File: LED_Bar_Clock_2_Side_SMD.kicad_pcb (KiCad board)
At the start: 2 copper layers, 100 x 100 mm, 52 parts, among them J1 U262-16XN-4BVC11, J2 AVR-ISP-6, SW1 SKHMQKE010, SW2 SW_5_Way, U1 ATtiny84A-SSUR, U2 DS1307Z+, Y1 32.768 kHz

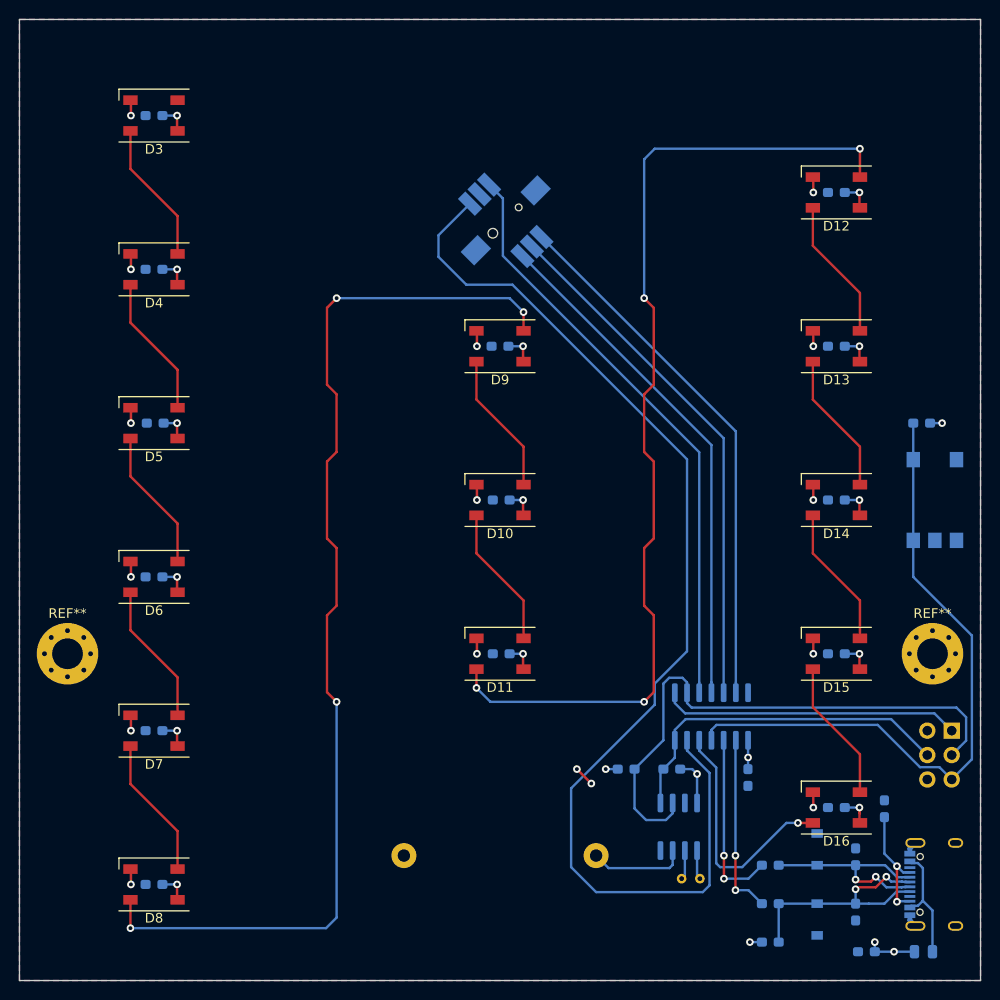
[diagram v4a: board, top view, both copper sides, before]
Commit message: Fix led and trace alignment
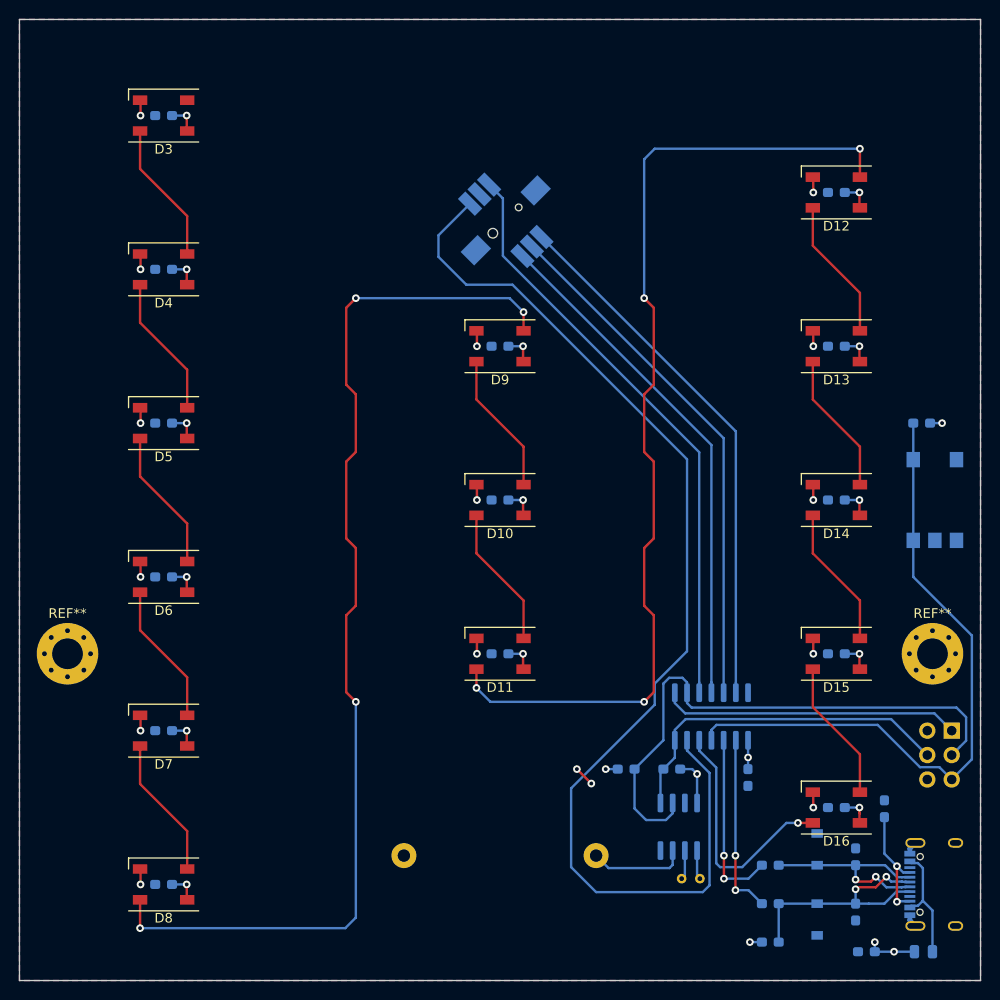
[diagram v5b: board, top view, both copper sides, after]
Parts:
- moved C4 1.00 mm to (65.0, 60.0)
- moved C5 1.00 mm to (65.0, 76.0)
- moved C7 1.00 mm to (65.0, 108.0)
- moved C8 1.00 mm to (65.0, 124.0)
- moved C9 1.00 mm to (65.0, 140.0)
- moved D3 1.00 mm to (65.0, 60.0)
- moved D4 1.00 mm to (65.0, 76.0)
- moved D5 1.00 mm to (65.0, 92.0)
- moved D6 1.00 mm to (65.0, 108.0)
- moved D7 1.00 mm to (65.0, 124.0)
- moved D8 1.00 mm to (65.0, 140.0)
- moved C6 0.88 mm to (65.0, 92.0)
- moved C11 0.12 mm to (100.0, 100.0)
- moved C12 0.12 mm to (100.0, 116.0)
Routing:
- net Net-(D8-Pad2): track 113.8 -> 112.8 mm

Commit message: Center 5 way switch
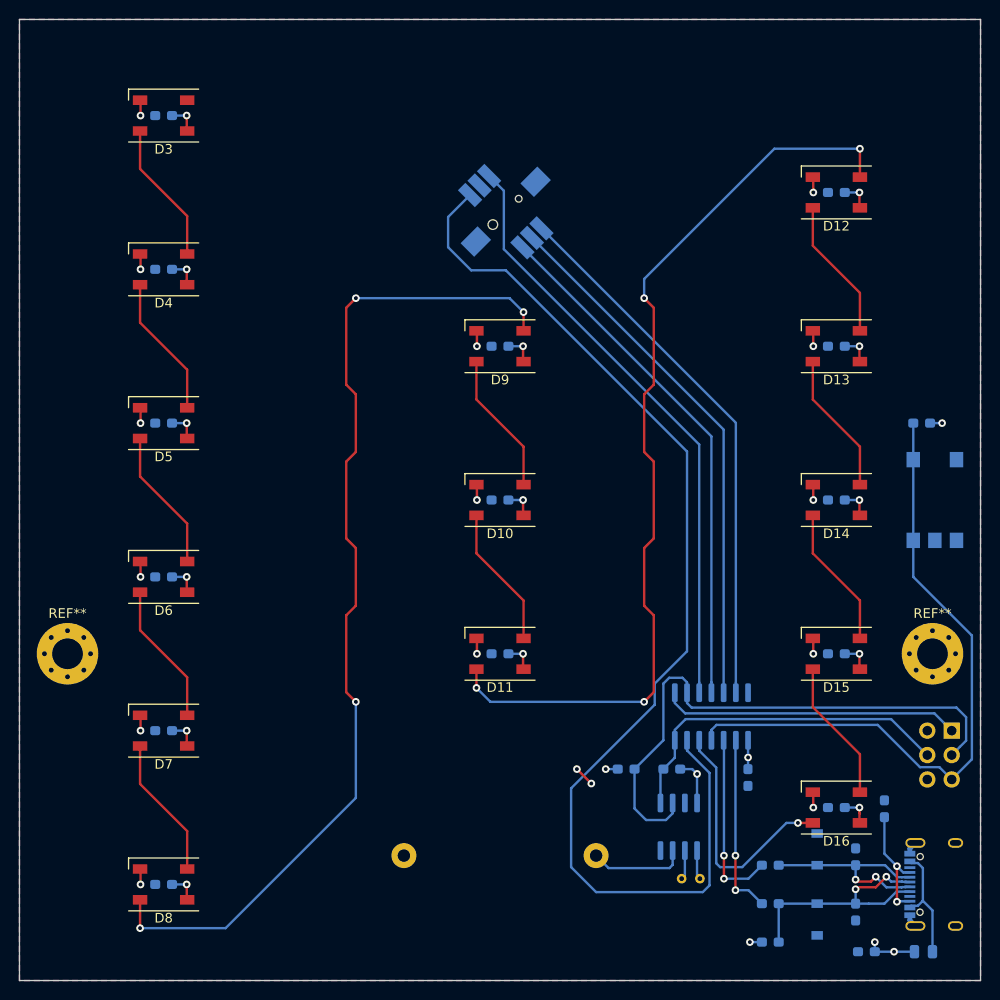
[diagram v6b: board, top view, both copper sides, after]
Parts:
- moved SW2 0.90 mm to (100.6, 70.0)
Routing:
- net Net-(D8-Pad2): track 112.8 -> 105.5 mm
- net Net-(D11-Pad2): track 104.8 -> 97.5 mm
- net Net-(SW2-Pad4): track 61.9 -> 62.8 mm
- net Net-(SW2-Pad3): track 53.6 -> 54.5 mm
- net Net-(SW2-Pad2): track 54.7 -> 55.6 mm
- net Net-(SW2-Pad1): track 55.8 -> 56.7 mm
- net Net-(SW2-Pad6): track 120.7 -> 120.1 mm
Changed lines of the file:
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@@
   )
   (module Clock_Footprints:K1-5203UA-01 (layer B.Cu)
-    (at 100.6 70.9 315)
+    (at 100.6 70 315)
     (fp_text reference SW2 (at 0.059999 0 315) (layer B.SilkS)
       (effects (font (size 1 1) (thickness 0.15)) (justify mirror))
@@
   (segment (start 102.45 82.4) (end 102.45 80.45) (width 0.25) (layer F.Cu) (net 12))
   (segment (start 101 79) (end 85 79) (width 0.25) (layer B.Cu) (net 12))
-  (segment (start 83.9 144.55) (end 62.55 144.55) (width 0.25) (layer B.Cu) (net 12))
-  (segment (start 85 121) (end 85 143.45) (width 0.25) (layer B.Cu) (net 12))
-  (segment (start 85 143.45) (end 83.9 144.55) (width 0.25) (layer B.Cu) (net 12))
+  (segment (start 71.45 144.55) (end 62.55 144.55) (width 0.25) (layer B.Cu) (net 12))
+  (segment (start 85 121) (end 85 131) (width 0.25) (layer B.Cu) (net 12))
+  (segment (start 85 131) (end 71.45 144.55) (width 0.25) (layer B.Cu) (net 12))
   (segment (start 97.55 89.55) (end 102.45 94.45) (width 0.25) (layer F.Cu) (net 13))
   (segment (start 102.45 94.45) (end 102.45 98.4) (width 0.25) (layer F.Cu) (net 13))
@@
   (via (at 137.45 63.45) (size 0.8) (drill 0.4) (layers F.Cu B.Cu) (net 15))
   (via (at 115 79) (size 0.8) (drill 0.4) (layers F.Cu B.Cu) (net 15))
-  (segment (start 116.1 63.45) (end 137.45 63.45) (width 0.25) (layer B.Cu) (net 15))
-  (segment (start 115 79) (end 115 64.55) (width 0.25) (layer B.Cu) (net 15))
-  (segment (start 115 64.55) (end 116.1 63.45) (width 0.25) (layer B.Cu) (net 15))
   (via (at 97.55 119.55) (size 0.8) (drill 0.4) (layers F.Cu B.Cu) (net 15))
   (segment (start 97.55 119.55) (end 97.55 117.6) (width 0.25) (layer F.Cu) (net 15))
@@
   (segment (start 99 121) (end 97.55 119.55) (width 0.25) (layer B.Cu) (net 15))
   (segment (start 115 121) (end 99 121) (width 0.25) (layer B.Cu) (net 15))
+  (segment (start 128.55 63.45) (end 137.45 63.45) (width 0.25) (layer B.Cu) (net 15))
+  (segment (start 115 79) (end 115 77) (width 0.25) (layer B.Cu) (net 15))
+  (segment (start 115 77) (end 128.55 63.45) (width 0.25) (layer B.Cu) (net 15))
   (segment (start 132.55 73.55) (end 137.45 78.45) (width 0.25) (layer F.Cu) (net 16))
   (segment (start 137.45 78.45) (end 137.45 82.4) (width 0.25) (layer F.Cu) (net 16))
@@
   (segment (start 139.3 123.4) (end 122.525 123.4) (width 0.25) (layer B.Cu) (net 28))
   (segment (start 122 123.925) (end 122 125) (width 0.25) (layer B.Cu) (net 28))
+  (segment (start 104.312311 71.732412) (end 124.54 91.960101) (width 0.25) (layer B.Cu) (net 29))
   (segment (start 124.54 118.975) (end 124.54 120.05) (width 0.25) (layer B.Cu) (net 29))
-  (segment (start 104.312311 72.632412) (end 124.54 92.860101) (width 0.25) (layer B.Cu) (net 29))
-  (segment (start 124.54 92.860101) (end 124.54 118.975) (width 0.25) (layer B.Cu) (net 29))
+  (segment (start 124.54 92) (end 124.54 118.975) (width 0.25) (layer B.Cu) (net 29))
+  (segment (start 102.332412 73.712311) (end 122 93.379899) (width 0.25) (layer B.Cu) (net 30))
   (segment (start 122 118.975) (end 122 120.05) (width 0.25) (layer B.Cu) (net 30))
-  (segment (start 102.332412 74.612311) (end 122 94.279899) (width 0.25) (layer B.Cu) (net 30))
-  (segment (start 122 94.279899) (end 122 118.975) (width 0.25) (layer B.Cu) (net 30))
-  (segment (start 123.27 93.57) (end 123.27 120.05) (width 0.25) (layer B.Cu) (net 31))
-  (segment (start 103.322361 73.622361) (end 123.27 93.57) (width 0.25) (layer B.Cu) (net 31))
+  (segment (start 122 93.4) (end 122 118.975) (width 0.25) (layer B.Cu) (net 30))
+  (segment (start 103.322361 72.722361) (end 123.27 92.67) (width 0.25) (layer B.Cu) (net 31))
+  (segment (start 123.27 92.7) (end 123.27 120.05) (width 0.25) (layer B.Cu) (net 31))
   (segment (start 120.73 118.975) (end 120.73 120.05) (width 0.25) (layer B.Cu) (net 32))
-  (segment (start 120.73 95.03) (end 120.73 118.975) (width 0.25) (layer B.Cu) (net 32))
-  (segment (start 100.3 74.6) (end 120.73 95.03) (width 0.25) (layer B.Cu) (net 32))
-  (segment (start 98.867588 67.187689) (end 100.3 68.620101) (width 0.25) (layer B.Cu) (net 32))
-  (segment (start 100.3 68.620101) (end 100.3 74.6) (width 0.25) (layer B.Cu) (net 32))
-  (segment (start 121.8 140.1) (end 121.1 140.8) (width 0.25) (layer B.Cu) (net 33))
-  (segment (start 119.46 126.06) (end 121.8 128.4) (width 0.25) (layer B.Cu) (net 33))
-  (segment (start 119.46 125) (end 119.46 126.06) (width 0.25) (layer B.Cu) (net 33))
-  (segment (start 121.8 128.4) (end 121.8 140.1) (width 0.25) (layer B.Cu) (net 33))
-  (segment (start 121.1 140.8) (end 110 140.8) (width 0.25) (layer B.Cu) (net 33))
-  (segment (start 110 140.8) (end 107.4 138.2) (width 0.25) (layer B.Cu) (net 33))
-  (segment (start 107.4 138.2) (end 107.4 130) (width 0.25) (layer B.Cu) (net 33))
-  (segment (start 107.4 130) (end 116.1 121.3) (width 0.25) (layer B.Cu) (net 33))
-  (segment (start 116.1 121.3) (end 116.1 119.1) (width 0.25) (layer B.Cu) (net 33))
-  (segment (start 116.1 119.1) (end 119.46 115.74) (width 0.25) (layer B.Cu) (net 33))
-  (segment (start 93.6 72.455277) (end 96.887689 69.167588) (width 0.25) (layer B.Cu) (net 33))
-  (segment (start 93.6 74.7) (end 93.6 72.455277) (width 0.25) (layer B.Cu) (net 33))
-  (segment (start 96.5 77.6) (end 93.6 74.7) (width 0.25) (layer B.Cu) (net 33))
-  (segment (start 101.3 77.6) (end 96.5 77.6) (width 0.25) (layer B.Cu) (net 33))
-  (segment (start 119.46 95.76) (end 101.3 77.6) (width 0.25) (layer B.Cu) (net 33))
-  (segment (start 119.46 115.74) (end 119.46 95.76) (width 0.25) (layer B.Cu) (net 33))
+  (segment (start 120.73 94.23) (end 120.73 118.975) (width 0.25) (layer B.Cu) (net 32))
+  (segment (start 100.4 73.9) (end 120.73 94.23) (width 0.25) (layer B.Cu) (net 32))
+  (segment (start 98.867588 66.287689) (end 100.4 67.820101) (width 0.25) (layer B.Cu) (net 32))
+  (segment (start 100.4 67.820101) (end 100.4 73.9) (width 0.25) (layer B.Cu) (net 32))
+  (segment (start 119.46 126.06) (end 119.46 125) (width 0.25) (layer B.Cu) (net 33))
+  (segment (start 121.8 128.4) (end 119.46 126.06) (width 0.25) (layer B.Cu) (net 33))
+  (segment (start 121.1 140.8) (end 121.8 140.1) (width 0.25) (layer B.Cu) (net 33))
+  (segment (start 110 140.8) (end 121.1 140.8) (width 0.25) (layer B.Cu) (net 33))
+  (segment (start 107.4 138.2) (end 110 140.8) (width 0.25) (layer B.Cu) (net 33))
+  (segment (start 107.4 130) (end 107.4 138.2) (width 0.25) (layer B.Cu) (net 33))
+  (segment (start 121.8 140.1) (end 121.8 128.4) (width 0.25) (layer B.Cu) (net 33))
+  (segment (start 116.1 121.3) (end 107.4 130) (width 0.25) (layer B.Cu) (net 33))
+  (segment (start 116.1 119.1) (end 116.1 121.3) (width 0.25) (layer B.Cu) (net 33))
+  (segment (start 94.6 70.555277) (end 94.6 73.7) (width 0.25) (layer B.Cu) (net 33))
+  (segment (start 96.887689 68.267588) (end 94.6 70.555277) (width 0.25) (layer B.Cu) (net 33))
+  (segment (start 119.46 115.74) (end 116.1 119.1) (width 0.25) (layer B.Cu) (net 33))
+  (segment (start 94.6 73.7) (end 97 76.1) (width 0.25) (layer B.Cu) (net 33))
+  (segment (start 97 76.1) (end 100.6 76.1) (width 0.25) (layer B.Cu) (net 33))
+  (segment (start 100.6 76.1) (end 119.46 94.96) (width 0.25) (layer B.Cu) (net 33))
+  (segment (start 119.46 94.96) (end 119.46 115.74) (width 0.25) (layer B.Cu) (net 33))
   (segment (start 120.505 139.105) (end 120.8 139.4) (width 0.25) (layer B.Cu) (net 34))
   (segment (start 120.505 136.475) (end 120.505 139.105) (width 0.25) (layer B.Cu) (net 34))
